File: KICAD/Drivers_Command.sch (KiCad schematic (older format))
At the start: 22 parts, among them U4 4011, U5 CD4053BM96, U6 CD4053BM96

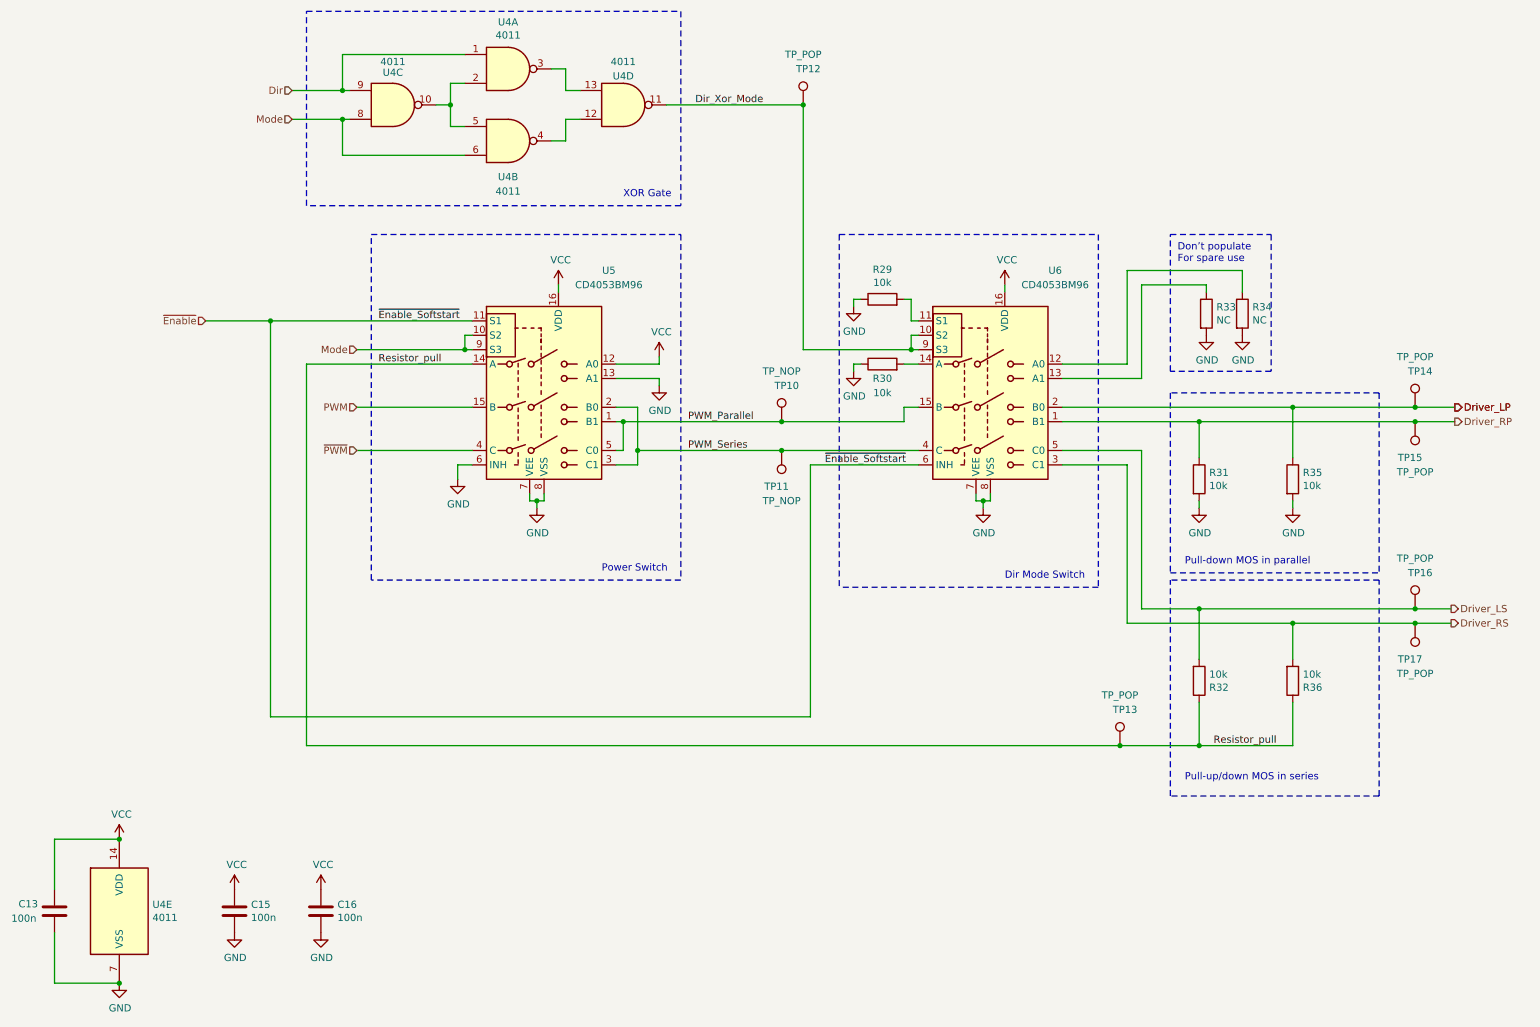
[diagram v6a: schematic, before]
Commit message: fixed a mistake w/ not connected net and net naming mistake
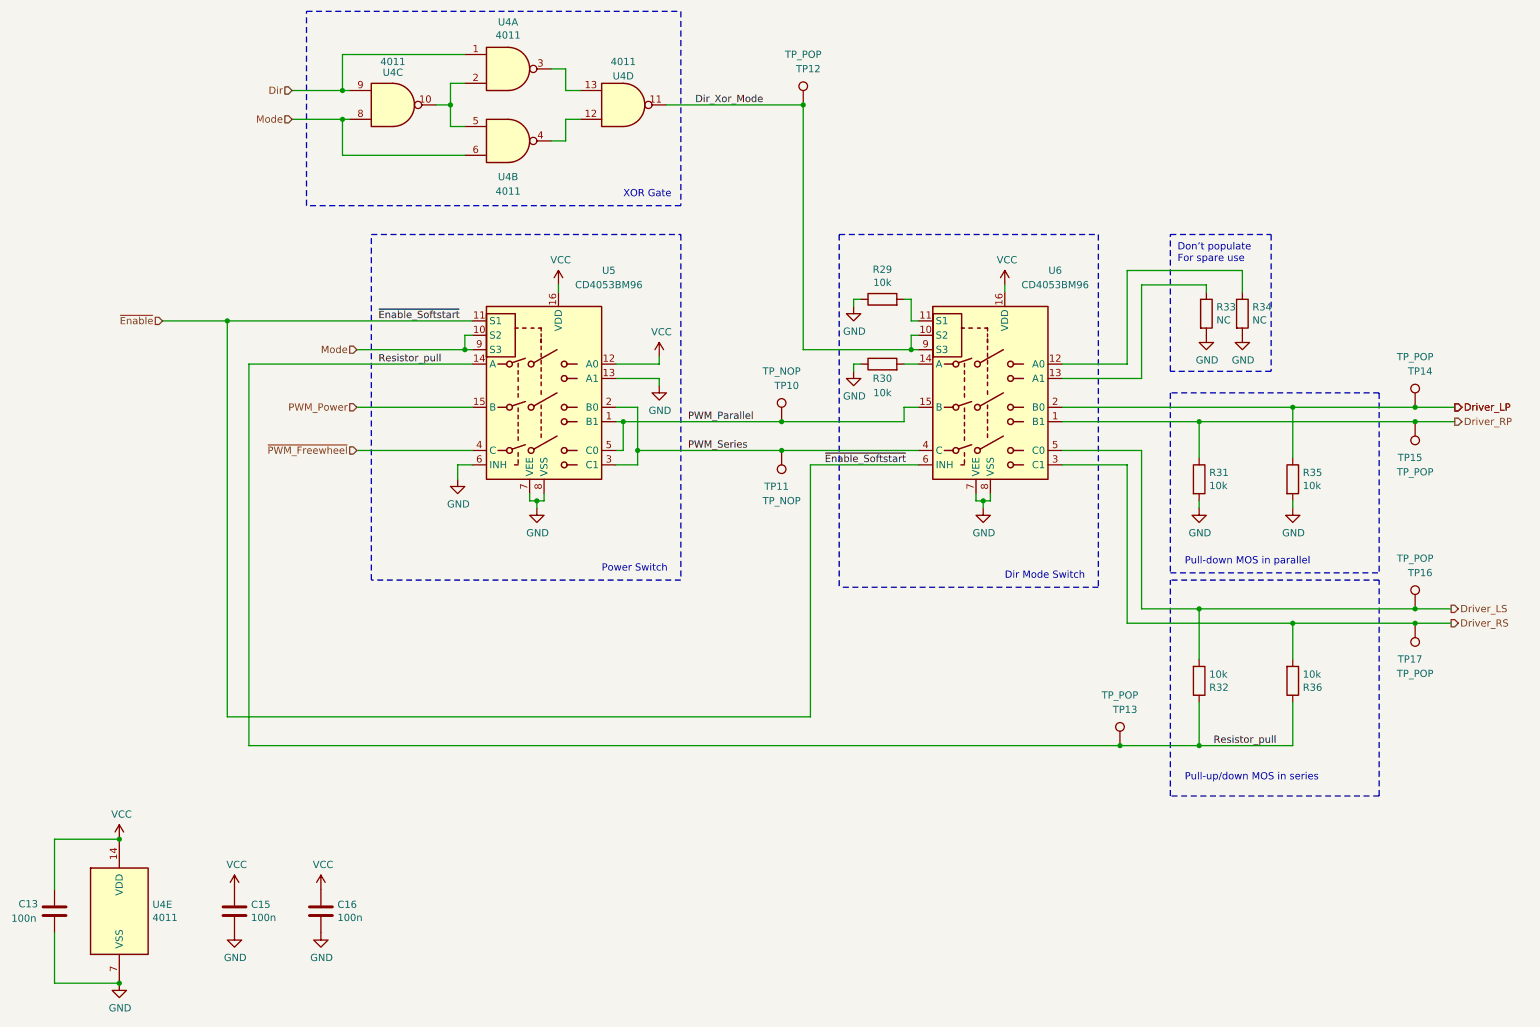
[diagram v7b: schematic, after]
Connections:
- net PWM renamed PWM_Power
- net ~PWM renamed ~PWM_Freewheel
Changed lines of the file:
@@
 	4200 4150 4250 4150
 Text HLabel 2950 3500 0    50   Input ~ 0
-PWM
+PWM_Power
 Text HLabel 2950 3800 0    50   Input ~ 0
-~PWM
+~PWM_Freewheel
 $Comp
 L sesame-fonctionnel-rescue:CD4053B-Analog_Switch U5
@@
 Connection ~ 8250 5850
 Wire Wire Line
-	8250 5850 2600 5850
+	8250 5850 2200 5850
 Text Label 6200 3900 0    50   ~ 0
 ~Enable_Softstart
@@
 	6100 3900 6100 5650
 Wire Wire Line
-	6100 5650 2350 5650
+	6100 5650 2050 5650
 Connection ~ 5900 3800
 Wire Wire Line
@@
 	5900 3600 6750 3600
 Wire Wire Line
-	2600 3200 2600 5850
-Wire Wire Line
-	2600 3200 3750 3200
-Wire Wire Line
-	2350 5650 2350 2900
-Wire Wire Line
-	2350 2900 3750 2900
+	2200 3200 2200 5850
+Wire Wire Line
+	2200 3200 3750 3200
+Wire Wire Line
+	2050 5650 2050 2900
+Wire Wire Line
+	2050 2900 3750 2900
 Text Notes 7450 4700 0    50   ~ 0
 Dir Mode Switch
@@
 Wire Notes Line
 	8100 4750 6300 4750
-Text HLabel 1900 2900 0    50   Input ~ 0
+Text HLabel 1600 2900 0    50   Input ~ 0
 ~Enable
 Connection ~ 1300 6500
 Wire Wire Line
-	1900 2900 2350 2900
-Connection ~ 2350 2900
+	1600 2900 2050 2900
+Connection ~ 2050 2900
 $EndSCHEMATC

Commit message: V1.0 of the schematic
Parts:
- U4: footprint Package_SO:SOIC-14_3.9x8.7mm_P1.27mm -> Sesame_footprint:SOIC-14_3.9x8.7mm_P1.27mm
- U5, U6: footprint Package_SO:SOIC-16_3.9x9.9mm_P1.27mm -> Sesame_footprint:SOIC-16_3.9x9.9mm_P1.27mm
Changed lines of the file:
@@
 Sheet 4 17
 Title "SESAME"
-Date "2021-08-04"
-Rev "A"
+Date "2021-09-23"
+Rev "1"
 Comp "ALEEA"
 Comment1 "Dessin : Clément & Josué & Guillaume Arthaud"
@@
 F 0 "U4" H 1530 7046 50  0000 L CNN
 F 1 "4011" H 1530 6955 50  0000 L CNN
-F 2 "Package_SO:SOIC-14_3.9x8.7mm_P1.27mm" H 1300 7000 50  0001 C CNN
+F 2 "Sesame_footprint:SOIC-14_3.9x8.7mm_P1.27mm" H 1300 7000 50  0001 C CNN
 F 3 "http://www.intersil.com/content/dam/Intersil/documents/cd40/cd4011bms-12bms-23bms.pdf" H 1300 7000 50  0001 C CNN
 	5    1300 7000
@@
 F 0 "U6" H 7800 4250 50  0000 C CNN
 F 1 "CD4053BM96" H 7800 4150 50  0000 C CNN
-F 2 "Package_SO:SOIC-16_3.9x9.9mm_P1.27mm" H 7500 2650 50  0001 L CNN
+F 2 "Sesame_footprint:SOIC-16_3.9x9.9mm_P1.27mm" H 7500 2650 50  0001 L CNN
 F 3 "" H 7330 3600 50  0001 C CNN
 	1    7350 3400
@@
 F 0 "U4" H 4000 1400 50  0000 C CNN
 F 1 "4011" H 4000 1300 50  0000 C CNN
-F 2 "Package_SO:SOIC-14_3.9x8.7mm_P1.27mm" H 4000 1650 50  0001 C CNN
+F 2 "Sesame_footprint:SOIC-14_3.9x8.7mm_P1.27mm" H 4000 1650 50  0001 C CNN
 F 3 "http://www.intersil.com/content/dam/Intersil/documents/cd40/cd4011bms-12bms-23bms.pdf" H 4000 1650 50  0001 C CNN
 	2    4000 1650
@@
 F 0 "U4" H 4800 1200 50  0000 C CNN
 F 1 "4011" H 4800 1100 50  0000 C CNN
-F 2 "Package_SO:SOIC-14_3.9x8.7mm_P1.27mm" H 4800 1400 50  0001 C CNN
+F 2 "Sesame_footprint:SOIC-14_3.9x8.7mm_P1.27mm" H 4800 1400 50  0001 C CNN
 F 3 "http://www.intersil.com/content/dam/Intersil/documents/cd40/cd4011bms-12bms-23bms.pdf" H 4800 1400 50  0001 C CNN
 	4    4800 1400
@@
 F 0 "U4" H 3200 1175 50  0000 C CNN
 F 1 "4011" H 3200 1100 50  0000 C CNN
-F 2 "Package_SO:SOIC-14_3.9x8.7mm_P1.27mm" H 3200 1400 50  0001 C CNN
+F 2 "Sesame_footprint:SOIC-14_3.9x8.7mm_P1.27mm" H 3200 1400 50  0001 C CNN
 F 3 "http://www.intersil.com/content/dam/Intersil/documents/cd40/cd4011bms-12bms-23bms.pdf" H 3200 1400 50  0001 C CNN
 	3    3200 1400
@@
 F 0 "U4" H 4000 1475 50  0000 C CNN
 F 1 "4011" H 4000 1384 50  0000 C CNN
-F 2 "Package_SO:SOIC-14_3.9x8.7mm_P1.27mm" H 4000 1150 50  0001 C CNN
+F 2 "Sesame_footprint:SOIC-14_3.9x8.7mm_P1.27mm" H 4000 1150 50  0001 C CNN
 F 3 "http://www.intersil.com/content/dam/Intersil/documents/cd40/cd4011bms-12bms-23bms.pdf" H 4000 1150 50  0001 C CNN
 	1    4000 1150
@@
 F 0 "U5" H 4700 4250 50  0000 C CNN
 F 1 "CD4053BM96" H 4700 4150 50  0000 C CNN
-F 2 "Package_SO:SOIC-16_3.9x9.9mm_P1.27mm" H 4400 2650 50  0001 L CNN
+F 2 "Sesame_footprint:SOIC-16_3.9x9.9mm_P1.27mm" H 4400 2650 50  0001 L CNN
 F 3 "" H 4230 3600 50  0001 C CNN
 	1    4250 3400
